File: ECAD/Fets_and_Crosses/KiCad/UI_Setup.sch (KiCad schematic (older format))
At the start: 15 parts, among them SW10 SW_DPDT_x2, SW11 SW_DPDT_x2, SW12 SW_Push

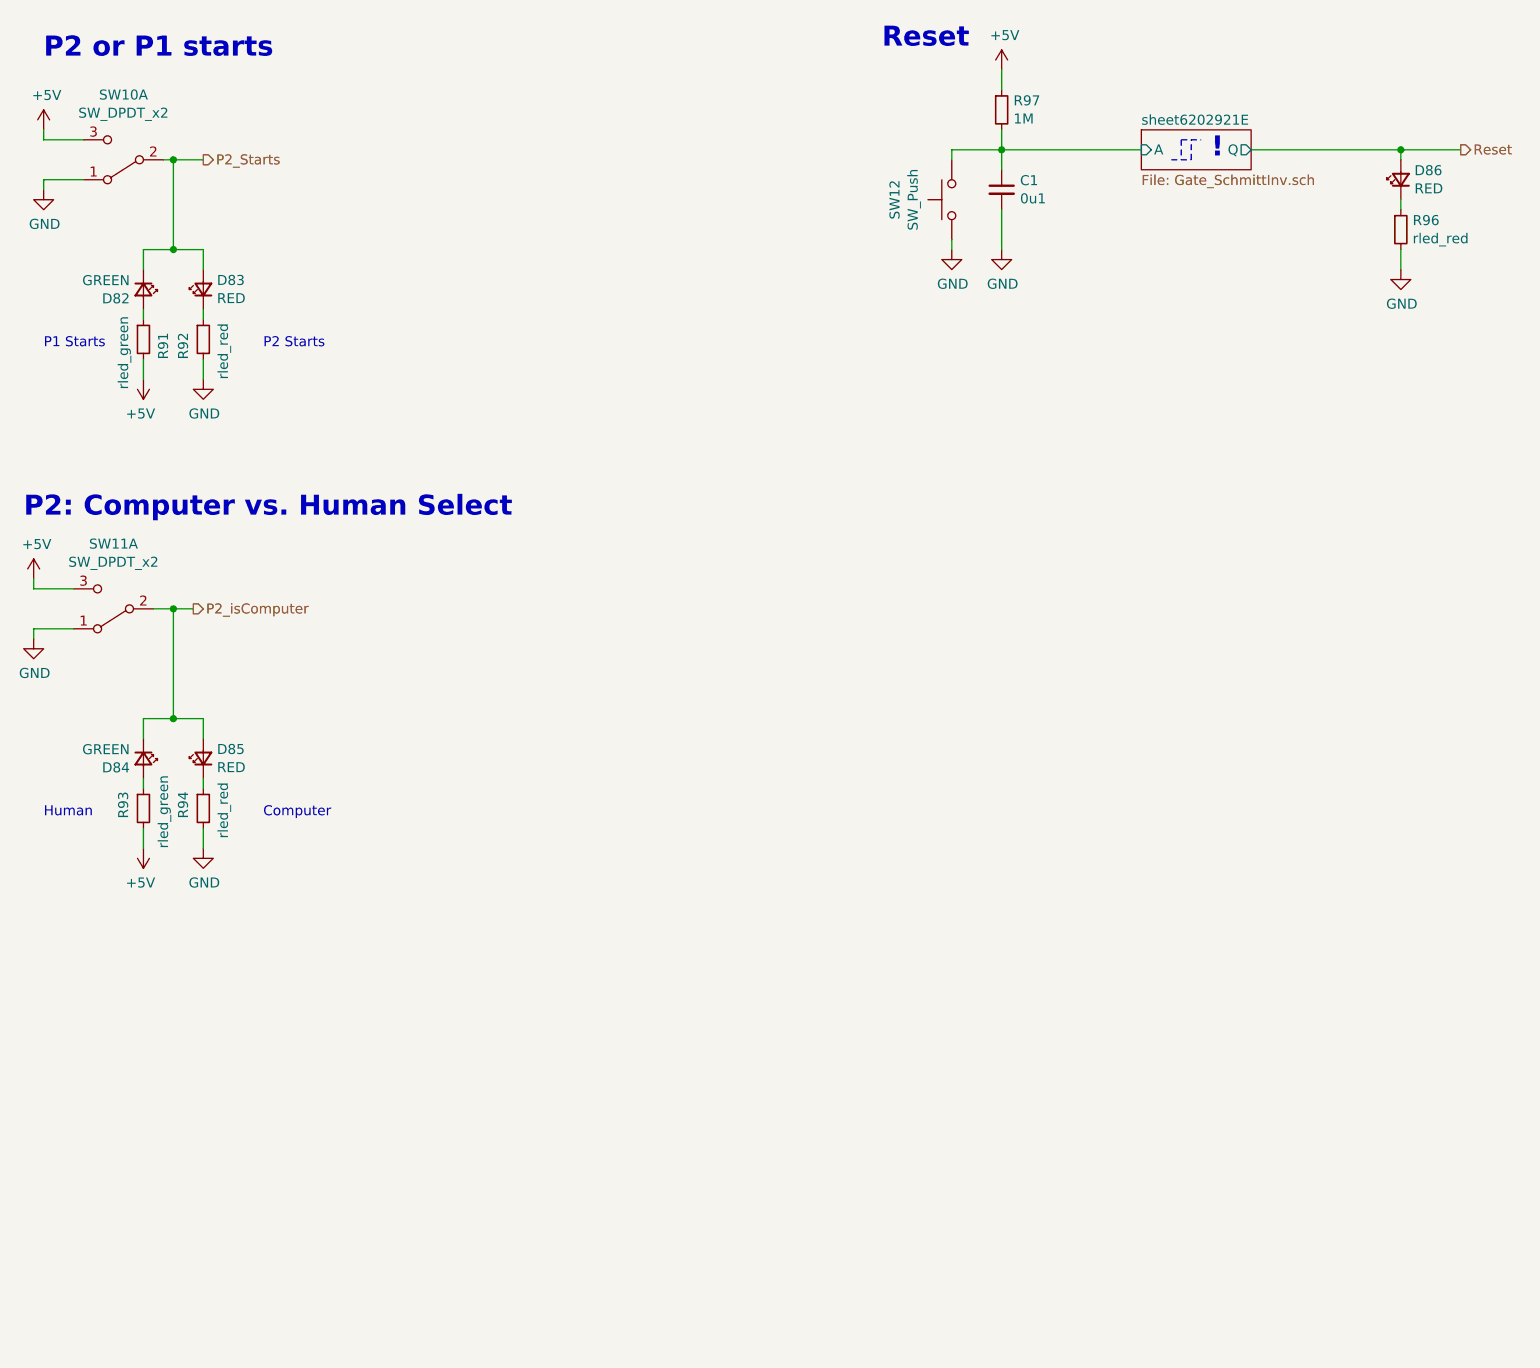
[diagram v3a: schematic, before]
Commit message: Specified LED Resisitors
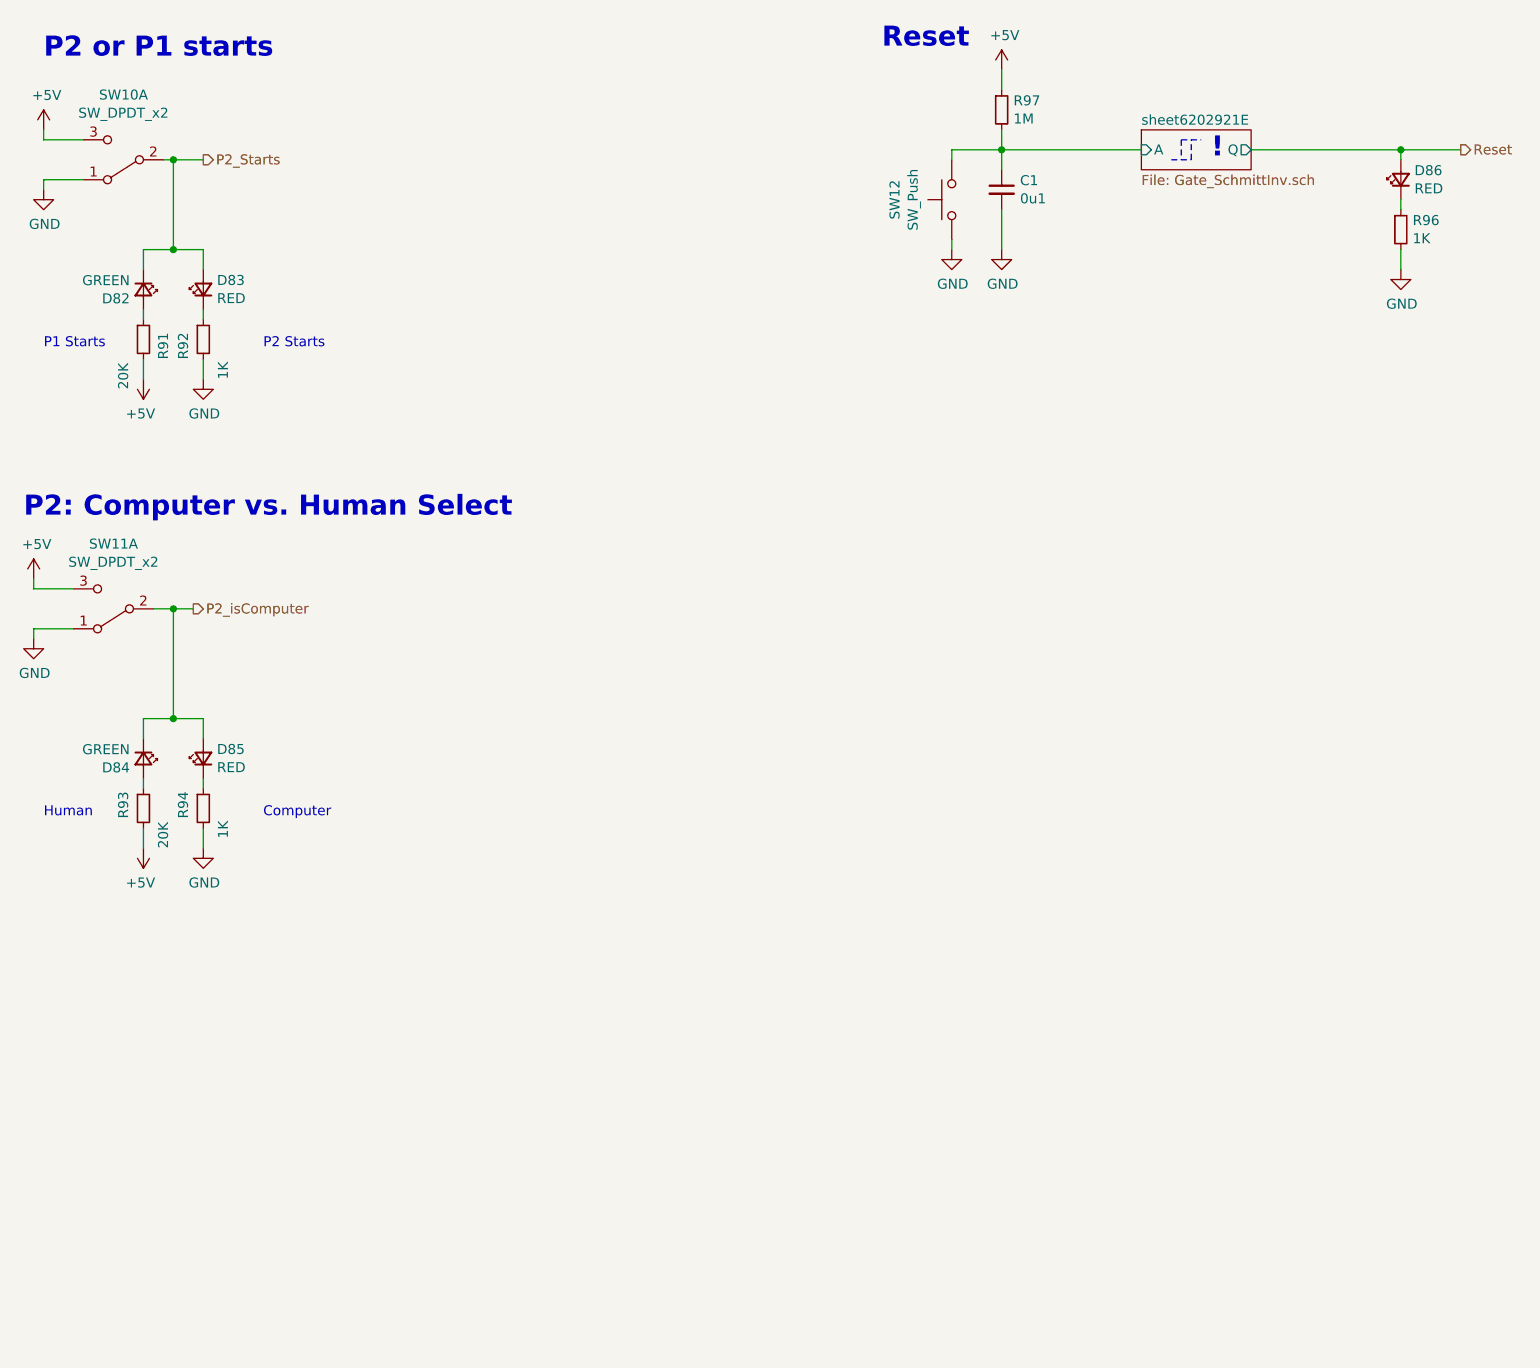
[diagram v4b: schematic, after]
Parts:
- R91, R93: value rled_green -> 20K; LCSC (none) -> C4184
- R92, R94, R96: value rled_red -> 1K; LCSC (none) -> C21190
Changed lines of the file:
@@
 AR Path="/5E53AD22/5E6A228F/5F0CF233" Ref="R91"  Part="1"
 F 0 "R91" V 2600 2150 50  0000 L CNN
-F 1 "rled_green" V 2400 2000 50  0000 L CNN
+F 1 "20K" V 2400 2000 50  0000 L CNN
 F 2 "LogicQ:R_0603_1608Metric_NOLBL" H 2500 2250 50  0001 C CNN
 F 3 "~" H 2500 2250 50  0001 C CNN
+F 4 "C4184" H 2500 2250 50  0001 C CNN "LCSC"
 	1    2500 2250
 	1    0    0    -1
@@
 AR Path="/5E53AD22/5E6A228F/5F0D1E2F" Ref="R92"  Part="1"
 F 0 "R92" V 2700 2150 50  0000 L CNN
-F 1 "rled_red" V 2900 2050 50  0000 L CNN
+F 1 "1K" V 2900 2050 50  0000 L CNN
 F 2 "LogicQ:R_0603_1608Metric_NOLBL" H 2800 2250 50  0001 C CNN
 F 3 "~" H 2800 2250 50  0001 C CNN
+F 4 "C21190" H 2800 2250 50  0001 C CNN "LCSC"
 	1    2800 2250
 	1    0    0    -1
@@
 AR Path="/5E53AD22/5E6A228F/5F0D5BDC" Ref="R93"  Part="1"
 F 0 "R93" V 2400 4550 50  0000 L CNN
-F 1 "rled_green" V 2600 4400 50  0000 L CNN
+F 1 "20K" V 2600 4400 50  0000 L CNN
 F 2 "LogicQ:R_0603_1608Metric_NOLBL" H 2500 4600 50  0001 C CNN
 F 3 "~" H 2500 4600 50  0001 C CNN
+F 4 "C4184" H 2500 4600 50  0001 C CNN "LCSC"
 	1    2500 4600
 	1    0    0    -1
@@
 AR Path="/5E53AD22/5E6A228F/5F0D5BEA" Ref="R94"  Part="1"
 F 0 "R94" V 2700 4550 50  0000 L CNN
-F 1 "rled_red" V 2900 4450 50  0000 L CNN
+F 1 "1K" V 2900 4450 50  0000 L CNN
 F 2 "LogicQ:R_0603_1608Metric_NOLBL" H 2800 4600 50  0001 C CNN
 F 3 "~" H 2800 4600 50  0001 C CNN
+F 4 "C21190" H 2800 4600 50  0001 C CNN "LCSC"
 	1    2800 4600
 	1    0    0    -1
@@
 AR Path="/5E53AD22/5E6A228F/5F0F0606" Ref="R96"  Part="1"
 F 0 "R96" H 8859 1746 50  0000 L CNN
-F 1 "rled_red" H 8859 1655 50  0000 L CNN
+F 1 "1K" H 8859 1655 50  0000 L CNN
 F 2 "LogicQ:R_0603_1608Metric_NOLBL" H 8800 1700 50  0001 C CNN
 F 3 "~" H 8800 1700 50  0001 C CNN
+F 4 "C21190" H 8800 1700 50  0001 C CNN "LCSC"
 	1    8800 1700
 	1    0    0    -1
